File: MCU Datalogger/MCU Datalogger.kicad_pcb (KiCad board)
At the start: 2 copper layers, 29 parts, among them J1 Conn_01x04_Pin, J2 Conn_01x09_Pin, J3 Conn_01x04_Pin, J4 Conn_02x03_Odd_Even, U1 24LC1025, U2 DS1337S_, U3 24LC1025, U4 ATMEGA328P-AU, Y1 32.768KHz, Y2 16MHz

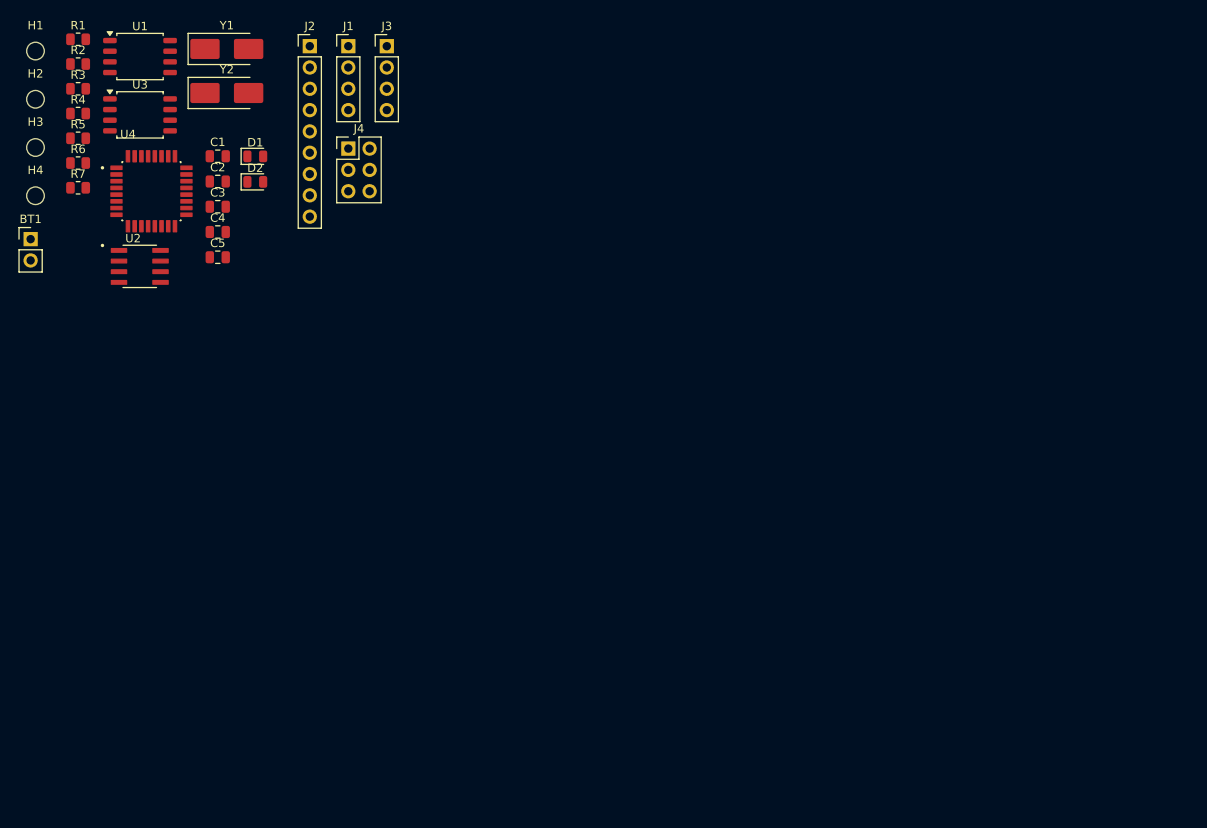
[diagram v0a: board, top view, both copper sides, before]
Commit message: 2layer: Completed placement of footprint
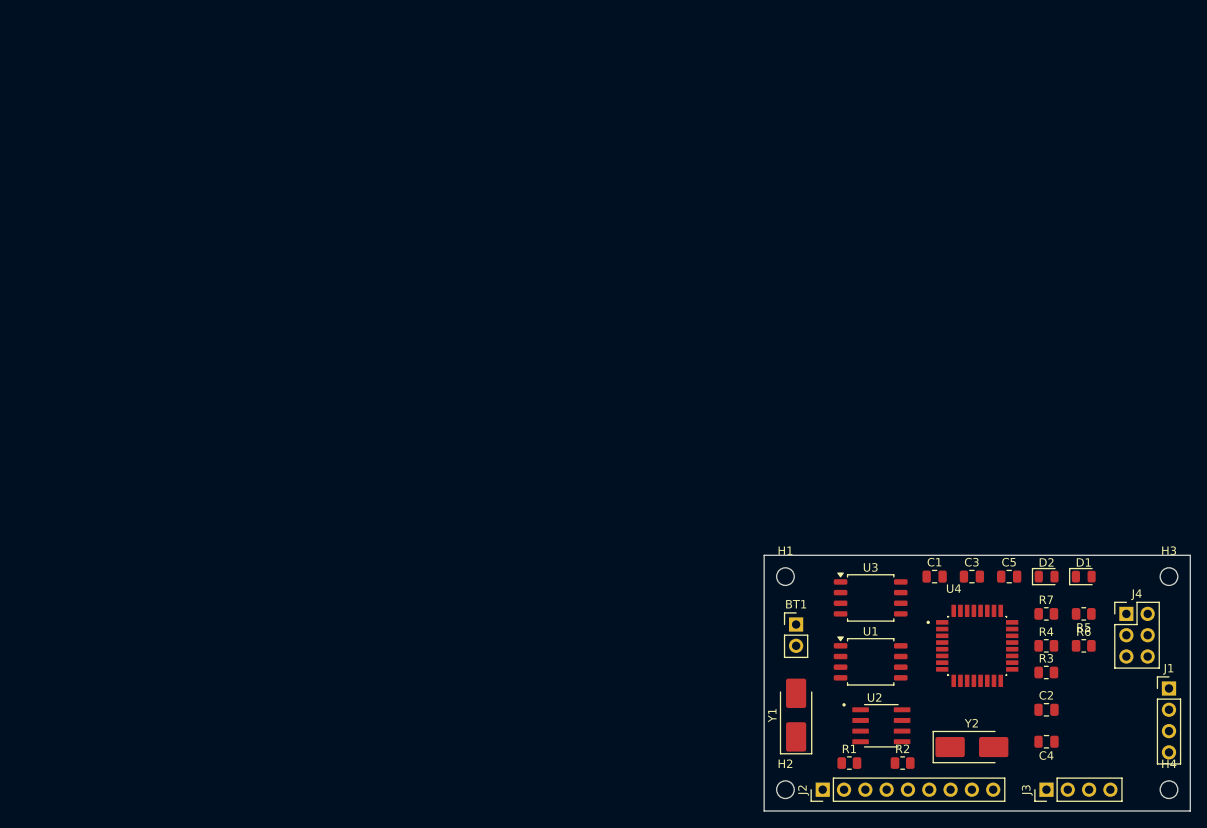
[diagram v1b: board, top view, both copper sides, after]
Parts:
- moved H4 152.5 mm to (161.3, 116.8)
- moved H3 144.5 mm to (161.3, 91.4)
- moved R3 134.8 mm to (146.7, 102.9)
- moved R6 133.0 mm to (151.1, 99.7)
- moved R5 132.6 mm to (151.1, 95.9), turned to 180 degrees
- moved R4 131.7 mm to (146.7, 99.7)
- moved R2 128.9 mm to (129.5, 113.7)
- moved R7 126.1 mm to (146.7, 95.9)
- moved R1 126.1 mm to (123.2, 113.7)
- moved J1 124.2 mm to (161.3, 104.8)
- moved H2 121.5 mm to (115.6, 116.8)
- moved J3 118.5 mm to (146.7, 116.8), turned to 90 degrees
- moved Y2 118.2 mm to (137.8, 111.8)
- moved C2 117.2 mm to (146.7, 107.3)
- moved C4 116.0 mm to (146.7, 111.1), turned to 180 degrees
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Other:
- board outline added: 50.8 x 30.5 mm

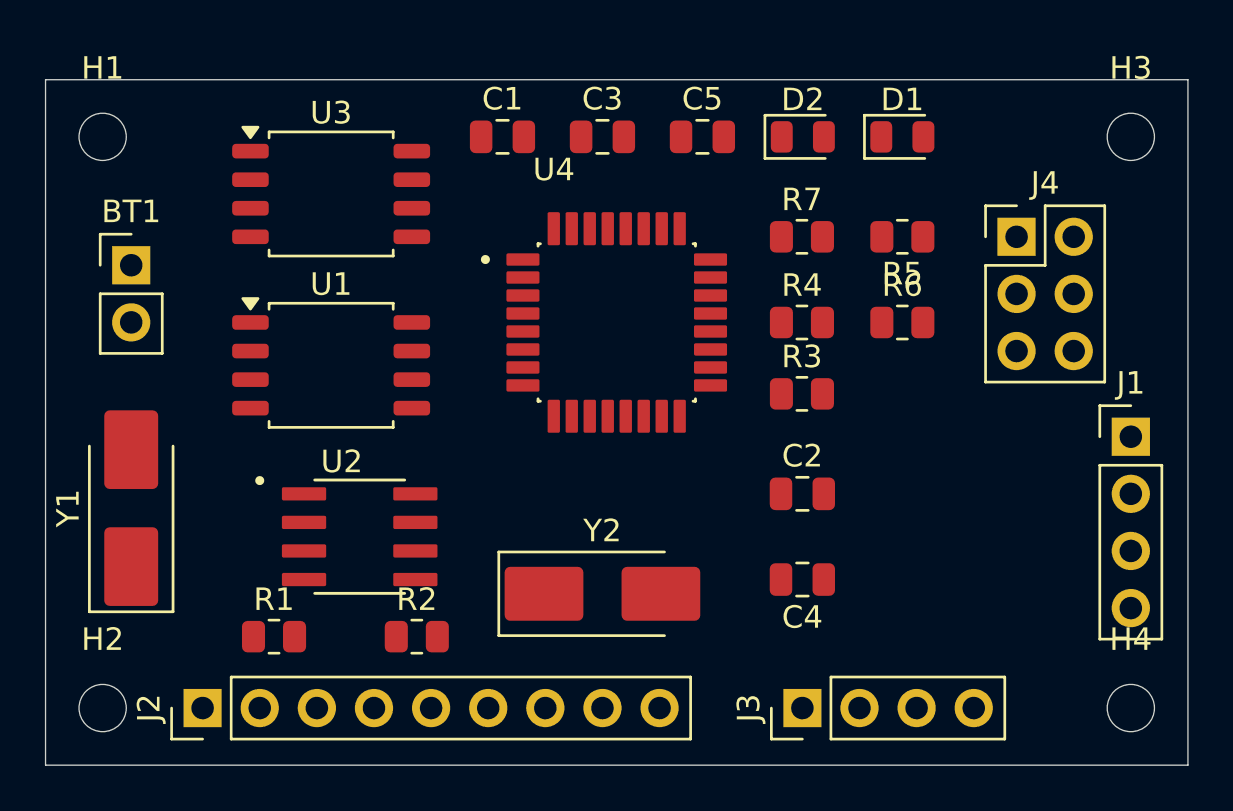
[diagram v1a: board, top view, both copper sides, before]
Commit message: 2layer: routing completed
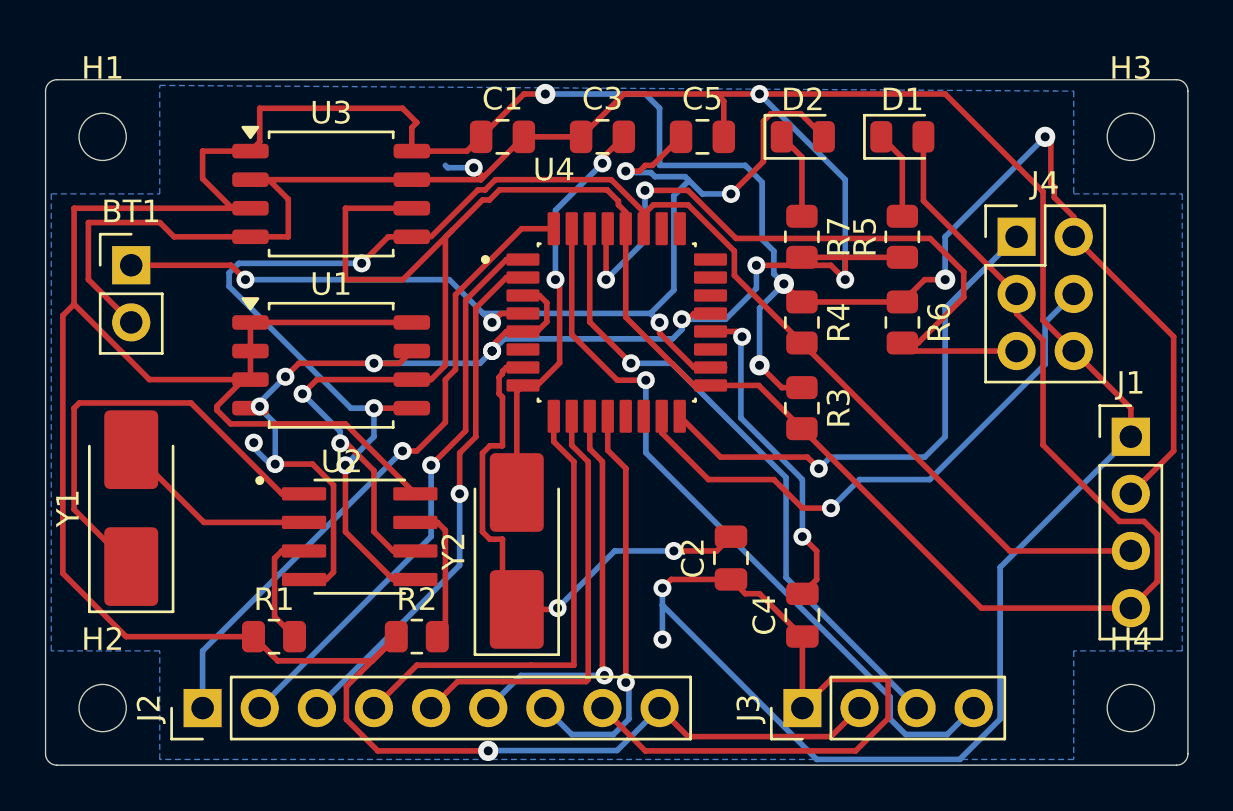
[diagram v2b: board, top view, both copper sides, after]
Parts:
- moved C2 4.27 mm to (143.5, 110.2), turned to 90 degrees
- moved Y2 4.26 mm to (134.0, 109.9), turned to 90 degrees
- moved C4 1.58 mm to (146.7, 112.7), turned to 90 degrees
- moved R3 0.63 mm to (146.7, 103.5), turned to -90 degrees
- turned R4 to -90 degrees
- turned R5 to 90 degrees
- turned R6 to -90 degrees
- turned R7 to -90 degrees
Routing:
- net GND: track 0.00 -> 206.4 mm, vias 0 -> 14
- net /Vcc: track 0.00 -> 185.4 mm, vias 0 -> 6
- net /SCK: track 0.00 -> 102.5 mm, vias 0 -> 2
- net /SDA: track 0.00 -> 71.1 mm, vias 0 -> 3
- net Net-(BT1-+): track 0.00 -> 52.6 mm, vias 0 -> 5
- net /TX: track 0.00 -> 33.5 mm, vias 0 -> 1
- net /RESET: track 0.00 -> 32.6 mm, vias 0 -> 2
- net /D2: track 0.00 -> 29.0 mm, vias 0 -> 1
- net /RX: track 0.00 -> 28.4 mm, vias 0 -> 1
- net /MOSI: track 0.00 -> 25.5 mm, vias 0 -> 1
- net /D3: track 0.00 -> 25.2 mm, vias 0 -> 1
- net Net-(U4-PB6): track 0.00 -> 24.2 mm, vias 0 -> 2
- net /MISO: track 0.00 -> 23.6 mm, vias 0 -> 1
- net /D4: track 0.00 -> 23.4 mm, vias 0 -> 1
- net /D5: track 0.00 -> 21.1 mm
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- added copper zone on B.Cu, net (none)
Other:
- outline, holes or cut-outs redrawn

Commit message: 2layer: refined routing
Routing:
- net GND: track 206.4 -> 201.6 mm, vias 14 -> 11
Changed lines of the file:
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@@
 		(tags "resistor")
 		(property "Reference" "R2"
-			(at 0 -1.65 0)
+			(at -2.794 -0.635 0)
 			(layer "F.SilkS")
 			(effects
@@
 			(at 1.27 7.46 0)
 			(layer "F.Fab")
+			(hide yes)
 			(effects
 				(font
@@
 			(at 0 -3.05 0)
 			(layer "F.SilkS")
+			(hide yes)
 			(effects
 				(font
@@
 			(at 0 3.05 0)
 			(layer "F.Fab")
+			(hide yes)
 			(effects
 				(font
@@
 			(at 0 10 90)
 			(layer "F.Fab")
+			(hide yes)
 			(effects
 				(font
@@
 			(at 0 -3.05 0)
 			(layer "F.SilkS")
+			(hide yes)
 			(effects
 				(font
@@
 			(at 0 3.05 0)
 			(layer "F.Fab")
+			(hide yes)
 			(effects
 				(font
@@
 		(tags "resistor")
 		(property "Reference" "R1"
-			(at 0 -1.65 0)
+			(at -1.016 -1.65 0)
 			(layer "F.SilkS")
 			(effects
@@
 			(at 0 -3.05 0)
 			(layer "F.SilkS")
+			(hide yes)
 			(effects
 				(font
@@
 			(at 0 3.05 0)
 			(layer "F.Fab")
+			(hide yes)
 			(effects
 				(font
@@
 			(at 0 3.05 0)
 			(layer "F.Fab")
+			(hide yes)
 			(effects
 				(font
@@
 			(at 0 10 0)
 			(layer "F.Fab")
+			(hide yes)
 			(effects
 				(font
@@
 			(at 0 22.7 90)
 			(layer "F.Fab")
+			(hide yes)
 			(effects
 				(font
@@
 	)
 	(segment
-		(start 133.525 100.095)
-		(end 132.888 100.732)
-		(width 0.25)
-		(layer "F.Cu")
-		(net 1)
-	)
-	(segment
 		(start 143.19 91.44)
 		(end 143.19 89.85)
@@
 	)
 	(segment
-		(start 132.395 93.136315)
-		(end 132.071444 92.812759)
-		(width 0.25)
-		(layer "F.Cu")
-		(net 1)
-	)
-	(segment
 		(start 147.95275 97.15275)
 		(end 144.64225 97.15275)
@@
 	)
 	(segment
-		(start 132.888 100.732)
-		(end 132.888 100.965)
+		(start 157.386 99.601)
+		(end 157.386 93.886)
 		(width 0.25)
 		(layer "F.Cu")
@@
 	)
 	(segment
-		(start 157.386 99.601)
-		(end 157.386 93.886)
+		(start 133.525 100.095)
+		(end 134.26 100.095)
 		(width 0.25)
 		(layer "F.Cu")
@@
 	)
 	(segment
-		(start 132.395 93.345)
-		(end 132.395 93.136315)
-		(width 0.25)
-		(layer "F.Cu")
-		(net 1)
-	)
-	(segment
 		(start 139.7 118.745)
 		(end 137.795 116.84)
@@
 	)
 	(segment
+		(start 132.888 100.732)
+		(end 133.525 100.095)
+		(width 0.25)
+		(layer "F.Cu")
+		(net 1)
+	)
+	(segment
 		(start 147.955 115.57)
 		(end 150.495 115.57)
@@
 	)
 	(segment
+		(start 132.888 100.965)
+		(end 132.888 100.732)
+		(width 0.25)
+		(layer "F.Cu")
+		(net 1)
+	)
+	(segment
 		(start 118.11 95.25)
 		(end 118.745 95.885)
@@
 	)
 	(segment
-		(start 134.26 100.095)
-		(end 133.525 100.095)
-		(width 0.25)
-		(layer "F.Cu")
-		(net 1)
-	)
-	(segment
 		(start 122.1425 93.345)
 		(end 122.954999 93.345)
@@
 	)
 	(via
-		(at 140.462 113.792)
-		(size 0.8)
-		(drill 0.4)
-		(layers "F.Cu" "B.Cu")
-		(net 1)
-	)
-	(via
 		(at 141.324952 99.553578)
 		(size 0.8)
@@
 	)
 	(via
-		(at 122.290153 105.039847)
-		(size 0.8)
-		(drill 0.4)
-		(layers "F.Cu" "B.Cu")
-		(net 1)
-	)
-	(via
 		(at 132.888 100.965)
 		(size 0.8)
@@
 	)
 	(via
-		(at 132.071444 92.812759)
-		(size 0.8)
-		(drill 0.4)
-		(layers "F.Cu" "B.Cu")
-		(net 1)
-	)
-	(via
 		(at 123.698 102.108)
 		(size 0.8)
@@
 	)
 	(segment
-		(start 132.071444 92.812759)
-		(end 130.912759 92.812759)
-		(width 0.25)
-		(layer "B.Cu")
-		(net 1)
-	)
-	(segment
 		(start 123.242653 105.992347)
 		(end 123.010347 105.992347)
@@
 	)
 	(segment
-		(start 132.888 100.965)
-		(end 132.343 101.51)
-		(width 0.25)
-		(layer "B.Cu")
-		(net 1)
-	)
-	(segment
-		(start 122.555 103.251)
-		(end 123.698 102.108)
+		(start 141.324952 100.009745)
+		(end 141.324952 99.553578)
 		(width 0.25)
 		(layer "B.Cu")
@@
 	)
 	(segment
-		(start 140.462 112.268)
-		(end 140.462 113.792)
+		(start 140.913697 100.421)
+		(end 141.324952 100.009745)
 		(width 0.25)
 		(layer "B.Cu")
@@
 	)
 	(segment
-		(start 141.324952 99.553578)
-		(end 141.324952 100.009745)
+		(start 122.555 103.251)
+		(end 123.698 102.108)
 		(width 0.25)
 		(layer "B.Cu")
@@
 	)
 	(segment
-		(start 141.324952 100.009745)
-		(end 140.913697 100.421)
-		(width 0.25)
-		(layer "B.Cu")
-		(net 1)
-	)
-	(segment
-		(start 130.912759 92.812759)
-		(end 130.81 92.71)
+		(start 132.888 100.965)
+		(end 132.343 101.51)
 		(width 0.25)
 		(layer "B.Cu")
@@
 	)
 	(segment
-		(start 148.59 97.79)
-		(end 148.59 93.345)
+		(start 133.432 100.421)
+		(end 140.913697 100.421)
 		(width 0.25)
 		(layer "B.Cu")
@@
 	)
 	(segment
-		(start 122.174 105.156)
-		(end 122.290153 105.039847)
+		(start 132.343 101.51)
+		(end 127.635 101.51)
 		(width 0.25)
 		(layer "B.Cu")
@@
 	)
 	(segment
-		(start 133.432 100.421)
-		(end 132.888 100.965)
+		(start 148.59 97.79)
+		(end 148.59 93.345)
 		(width 0.25)
 		(layer "B.Cu")
@@
 	)
 	(segment
-		(start 122.555 103.505)
-		(end 122.555 103.431)
+		(start 132.888 100.965)
+		(end 133.432 100.421)
 		(width 0.25)
 		(layer "B.Cu")
@@
 	)
 	(segment
-		(start 123.010347 105.992347)
-		(end 122.174 105.156)
+		(start 122.555 103.505)
+		(end 122.555 103.431)
 		(width 0.25)
 		(layer "B.Cu")
@@
 	)
 	(segment
-		(start 140.913697 100.421)
-		(end 133.432 100.421)
-		(width 0.25)
-		(layer "B.Cu")
-		(net 1)
-	)
-	(segment
 		(start 140.462 112.268)
 		(end 147.32 119.126)
@@
 		(width 0.25)
 		(layer "B.Cu")
-		(net 1)
-	)
-	(segment
-		(start 132.343 101.51)
-		(end 127.635 101.51)
-		(width 0.25)
-		(layer "B.Cu")

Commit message: 2layer: routing and silkscreen complete
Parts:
- added REF**: KiCad-Logo2_5mm_SilkScreen, Symbol:KiCad-Logo2_5mm_SilkScreen, B.Cu at (126.4, 94.6)
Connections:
- BT1 pad 1: Net-(BT1-+) -> /Vcc
- C5 pad 1: Net-(BT1-+) -> /Vcc
- D2 pad 2: Net-(BT1-+) -> /Vcc
- U4 pad 18: Net-(BT1-+) -> /Vcc
- U4 pad 4: Net-(BT1-+) -> /Vcc
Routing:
- net /Vcc: track 185.4 -> 240.0 mm, vias 6 -> 11
- net Net-(BT1-+): track 52.6 -> 0.00 mm, vias 5 -> 0
- net GND: track 201.6 -> 208.0 mm, vias 11 -> 10
- net Net-(U4-PB7): track 18.3 -> 22.5 mm
- net /TX: track 33.5 -> 34.0 mm
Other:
- board text added: "- 2Mbit EEPROM - RTC - I2C, SPI, GPIOs"
- board text added: "2"
- board text added: "3"
- board text added: "4"
- board text added: "5"
- board text added: "6"
- board text added: "7"
- board text added: "8"
- board text added: "Data logger with the ATMEGA328P."
- board text added: "GND"
- board text added: "GPIO"
- board text added: "I2C"
- board text added: "ICSP"
- board text added: "ICSP MISO | VCC SCK | MOSI RESET| GND"
- board text added: "RX"
- board text added: "SCK"
- board text added: "SDA"
- board text added: "SERIAL"
- board text added: "TX"
- board text added: "VCC"

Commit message: 2layer: Completed 2 layer pcb project and added gerber for manufacturing
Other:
- board text added: "0.2000 mm / 0.0000 mm"
- board text added: "0.3000 mm"
- board text added: "1.6000 mm"
- board text added: "50.8000 mm x 30.4800 mm"
- board text added: "BOARD CHARACTERISTICS"
- board text added: "Board Thickness:"
- board text added: "Board overall dimensions:"
- board text added: "Castellated pads:"
- board text added: "Copper Finish:"
- board text added: "Copper Layer Count:"
- board text added: "Edge card connectors:"
- board text added: "Impedance Control:"
- board text added: "Min hole diameter:"
- board text added: "Min track/spacing:"
- board text added: "No"
- board text added: "None"
- board text added: "Plated Board Edge:"
